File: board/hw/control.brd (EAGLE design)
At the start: 54.3 x 82.5 mm, 34 parts, among them T1 pn2222a, T2 pn2222a, T3 pn2222a, T4 pn2222a, T5 pn2222a, T6 pn2222a, T7 pn2222a, T8 pn2222a

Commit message: added missing power supply connector
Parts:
- added SV3: (no value), con-amp-mt:S02P
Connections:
- net +5V: now also SV3.1
- net 0V: now also SV3.2
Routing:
- net +5V: track 167.1 -> 177.8 mm
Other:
- board text added: "+5V"
- board text added: "GND"
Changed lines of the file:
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@@
 control board
 v1.0</text>
+<text x="86.995" y="58.42" size="1.778" layer="51" rot="R90">+5V</text>
+<text x="86.995" y="50.165" size="1.778" layer="51" rot="R90">GND</text>
 </plain>
 <attributes>
@@
 <element name="T1" library="transistor" package="TO92-CBE" value="pn2222a" x="73.66" y="62.23" smashed="yes">
 <attribute name="NAME" x="71.12" y="65.278" size="1.27" layer="25" ratio="10"/>
-<attribute name="VALUE" x="77.47" y="61.468" size="1.27" layer="27" ratio="10"/>
+<attribute name="VALUE" x="77.47" y="62.738" size="1.27" layer="27" ratio="10"/>
 </element>
 <element name="T2" library="transistor" package="TO92-CBE" value="pn2222a" x="71.12" y="54.61" smashed="yes">
@@
 <attribute name="NAME" x="44.45" y="35.179" size="1.27" layer="25" ratio="10" rot="R270"/>
 <attribute name="VALUE" x="44.323" y="46.609" size="1.27" layer="27" ratio="10" rot="R270"/>
+</element>
+<element name="SV3" library="con-amp-mt" package="S02P" value="" x="82.55" y="55.88" rot="R90">
+<attribute name="MPN" value="" x="82.55" y="55.88" size="1.778" layer="27" rot="R90" display="off"/>
+<attribute name="MF" value="" x="82.55" y="55.88" size="1.778" layer="27" rot="R90" display="off"/>
+<attribute name="OC_FARNELL" value="unknown" x="82.55" y="55.88" size="1.778" layer="27" rot="R90" display="off"/>
+<attribute name="OC_NEWARK" value="unknown" x="82.55" y="55.88" size="1.778" layer="27" rot="R90" display="off"/>
 </element>
 </elements>
@@
 <wire x1="40.64" y1="54.61" x2="40.64" y2="57.15" width="0.4064" layer="16"/>
 <wire x1="40.64" y1="57.15" x2="53.34" y2="69.85" width="0.4064" layer="16"/>
+<contactref element="SV3" pad="1"/>
+<wire x1="81.28" y1="67.31" x2="81.28" y2="58.4" width="0.4064" layer="16"/>
+<wire x1="81.28" y1="58.4" x2="82.55" y2="57.13" width="0.4064" layer="16"/>
 </signal>
 <signal name="0V">
@@
 <vertex x="35.56" y="80.01"/>
 </polygon>
+<contactref element="SV3" pad="2"/>
 </signal>
 <signal name="N$8">

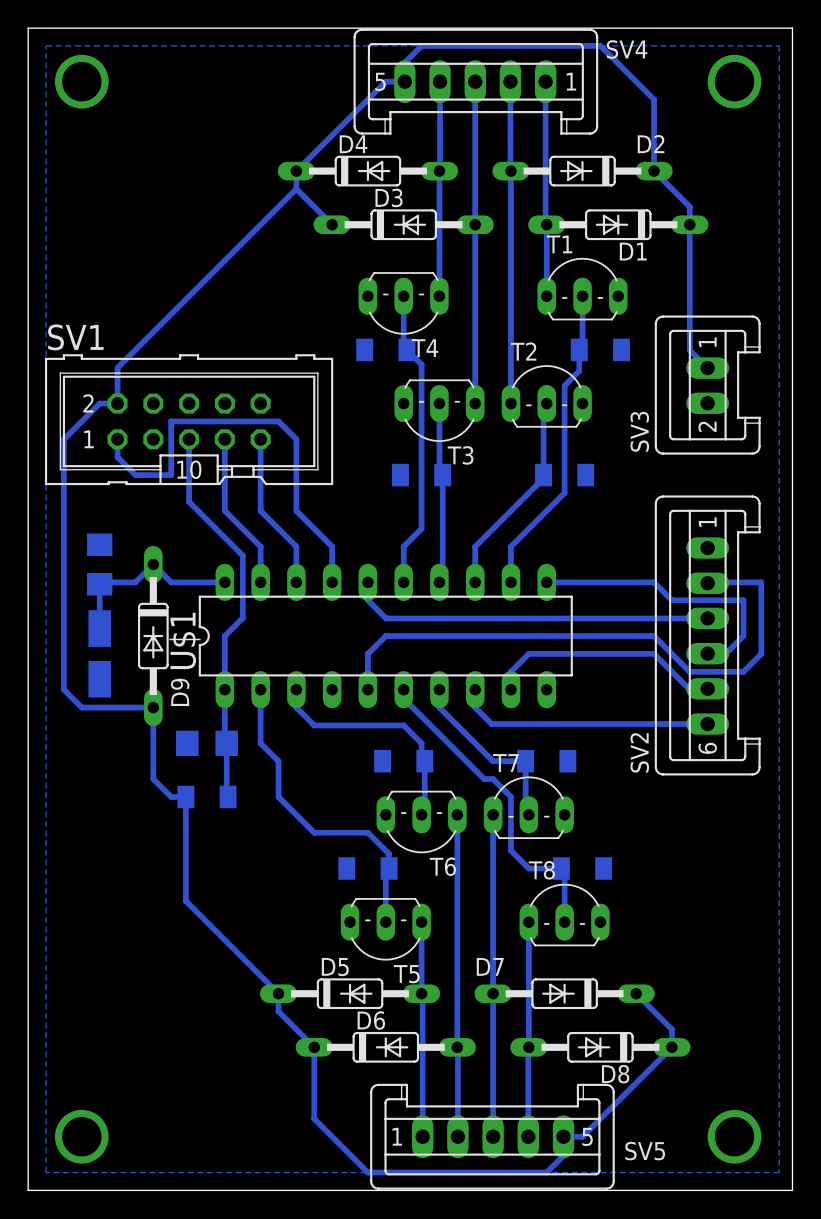
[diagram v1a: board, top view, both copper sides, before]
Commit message: added missing pull-up 100k Rs for all buttons
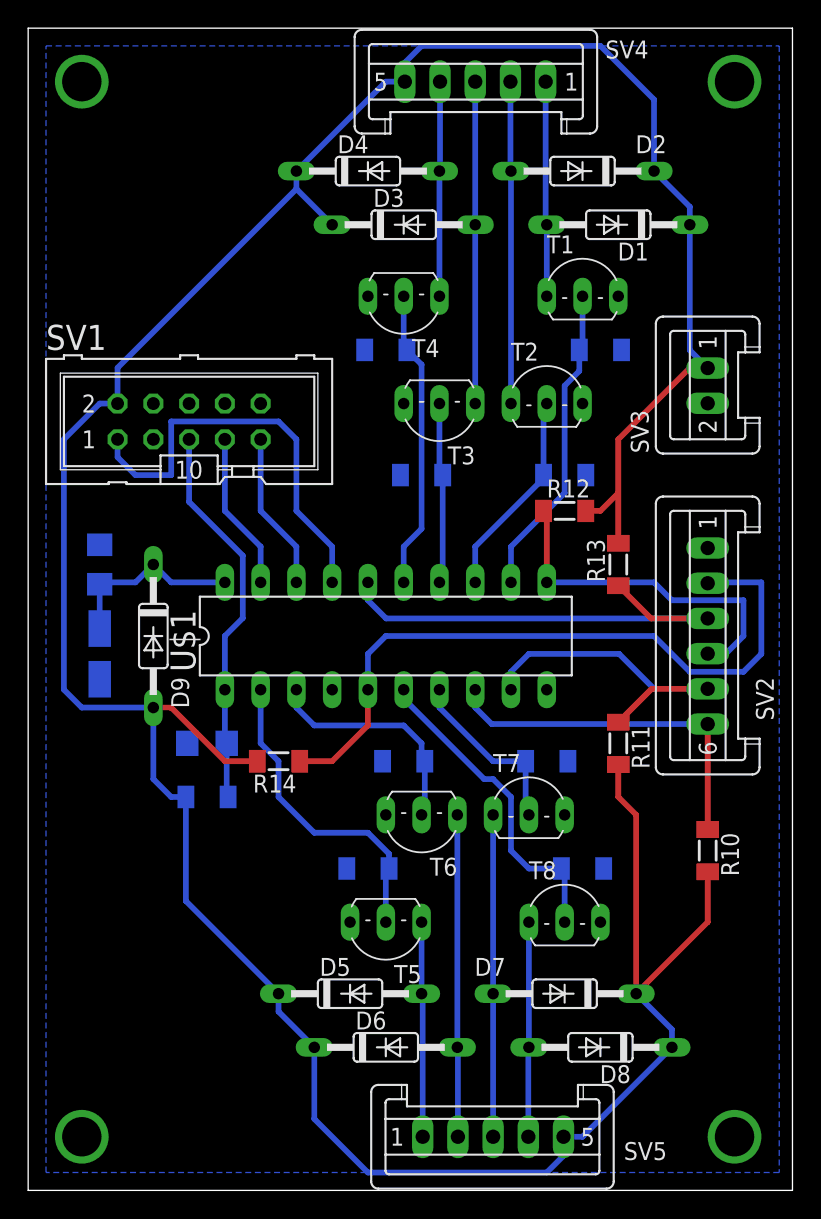
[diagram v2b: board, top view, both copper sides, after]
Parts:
- added R10, R11, R12, R13, R14: 100kR, rcl:MINI_MELF-0204W
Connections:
- net +5V: now also R10.2, R11.2, R12.2, R13.2, R14.2
- net N$22: now also R11.1
- net N$23: now also R12.1
- net N$24: now also R13.1
- net N$25: now also R14.1
- net N$3: now also R10.1
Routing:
- net +5V: track 177.8 -> 233.1 mm
- net N$25: track 41.5 -> 49.9 mm
- net N$3: track 18.3 -> 25.8 mm
- net N$22: track 16.8 -> 24.1 mm
- net N$24: track 25.9 -> 33.2 mm
- net N$23: track 20.1 -> 25.3 mm
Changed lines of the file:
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@@
 </element>
 <element name="D8" library="diode" package="DO35-10" value="1N4446" x="74.93" y="8.89" rot="R180"/>
-<element name="SV2" library="con-amp-mt" package="S06P" value="buttons" x="82.55" y="38.1" rot="R90">
+<element name="SV2" library="con-amp-mt" package="S06P" value="buttons" x="82.55" y="38.1" smashed="yes" rot="R90">
 <attribute name="MPN" value="" x="82.55" y="38.1" size="1.778" layer="27" rot="R90" display="off"/>
 <attribute name="MF" value="" x="82.55" y="38.1" size="1.778" layer="27" rot="R90" display="off"/>
 <attribute name="OC_NEWARK" value="unknown" x="82.55" y="38.1" size="1.778" layer="27" rot="R90" display="off"/>
 <attribute name="OC_FARNELL" value="unknown" x="82.55" y="38.1" size="1.778" layer="27" rot="R90" display="off"/>
+<attribute name="NAME" x="87.249" y="32.1072" size="1.27" layer="25" ratio="10" rot="R90"/>
+<attribute name="VALUE" x="78.359" y="35.4092" size="1.27" layer="27" ratio="10" rot="R90"/>
 </element>
 <element name="D9" library="diode" package="DO35-10" value="1N4446" x="43.18" y="38.1" smashed="yes" rot="R270">
@@
 <attribute name="OC_NEWARK" value="unknown" x="82.55" y="55.88" size="1.778" layer="27" rot="R90" display="off"/>
 </element>
+<element name="R10" library="rcl" package="MINI_MELF-0204W" value="100kR" x="82.55" y="22.86" rot="R270"/>
+<element name="R11" library="rcl" package="MINI_MELF-0204W" value="100kR" x="76.2" y="30.48" rot="R270"/>
+<element name="R12" library="rcl" package="MINI_MELF-0204W" value="100kR" x="72.39" y="46.99"/>
+<element name="R13" library="rcl" package="MINI_MELF-0204W" value="100kR" x="76.2" y="43.18" rot="R90"/>
+<element name="R14" library="rcl" package="MINI_MELF-0204W" value="100kR" x="52.07" y="29.21" rot="R180"/>
 </elements>
 <signals>
@@
 <wire x1="81.28" y1="67.31" x2="81.28" y2="58.4" width="0.4064" layer="16"/>
 <wire x1="81.28" y1="58.4" x2="82.55" y2="57.13" width="0.4064" layer="16"/>
+<contactref element="R10" pad="2"/>
+<contactref element="R11" pad="2"/>
+<contactref element="R12" pad="2"/>
+<contactref element="R13" pad="2"/>
+<contactref element="R14" pad="2"/>
+<wire x1="82.55" y1="21.36" x2="82.55" y2="17.78" width="0.4064" layer="1"/>
+<wire x1="82.55" y1="17.78" x2="77.47" y2="12.7" width="0.4064" layer="1"/>
+<wire x1="76.2" y1="26.67" x2="77.47" y2="25.4" width="0.4064" layer="1"/>
+<wire x1="77.47" y1="25.4" x2="77.47" y2="12.7" width="0.4064" layer="1"/>
+<wire x1="44.45" y1="33.02" x2="43.18" y2="33.02" width="0.4064" layer="1"/>
+<wire x1="76.2" y1="44.68" x2="76.2" y2="48.26" width="0.4064" layer="1"/>
+<wire x1="76.2" y1="48.26" x2="76.2" y2="52.07" width="0.4064" layer="1"/>
+<wire x1="76.2" y1="52.07" x2="81.28" y2="57.15" width="0.4064" layer="1"/>
+<wire x1="81.28" y1="57.15" x2="82.53" y2="57.15" width="0.4064" layer="1"/>
+<wire x1="82.53" y1="57.15" x2="82.55" y2="57.13" width="0.4064" layer="1"/>
+<wire x1="73.89" y1="46.99" x2="74.93" y2="46.99" width="0.4064" layer="1"/>
+<wire x1="74.93" y1="46.99" x2="76.2" y2="48.26" width="0.4064" layer="1"/>
+<wire x1="76.2" y1="28.98" x2="76.2" y2="26.67" width="0.4064" layer="1"/>
+<wire x1="50.57" y1="29.21" x2="48.26" y2="29.21" width="0.4064" layer="1"/>
+<wire x1="48.26" y1="29.21" x2="44.45" y2="33.02" width="0.4064" layer="1"/>
 </signal>
 <signal name="0V">
@@
 <wire x1="67.21" y1="31.85" x2="66.04" y2="33.02" width="0.4064" layer="16"/>
 <wire x1="66.04" y1="33.02" x2="66.04" y2="34.29" width="0.4064" layer="16"/>
+<contactref element="R10" pad="1"/>
+<wire x1="82.55" y1="24.36" x2="82.55" y2="31.85" width="0.4064" layer="1"/>
 </signal>
 <signal name="N$22">
 <contactref element="SV2" pad="5"/>
 <contactref element="U$1" pad="9"/>
-<wire x1="82.55" y1="34.35" x2="81.22" y2="34.35" width="0.4064" layer="16"/>
-<wire x1="81.22" y1="34.35" x2="78.74" y2="36.83" width="0.4064" layer="16"/>
-<wire x1="78.74" y1="36.83" x2="69.85" y2="36.83" width="0.4064" layer="16"/>
-<wire x1="69.85" y1="36.83" x2="68.58" y2="35.56" width="0.4064" layer="16"/>
-<wire x1="68.58" y1="35.56" x2="68.58" y2="34.29" width="0.4064" layer="16"/>
+<contactref element="R11" pad="1"/>
+<wire x1="82.55" y1="34.35" x2="78.57" y2="34.35" width="0.4064" layer="1"/>
+<wire x1="78.57" y1="34.35" x2="76.2" y2="31.98" width="0.4064" layer="1"/>
+<wire x1="68.58" y1="34.29" x2="68.58" y2="35.56" width="0.4064" layer="16"/>
+<wire x1="68.58" y1="35.56" x2="69.85" y2="36.83" width="0.4064" layer="16"/>
+<wire x1="69.85" y1="36.83" x2="76.26" y2="36.83" width="0.4064" layer="16"/>
+<wire x1="76.26" y1="36.83" x2="78.74" y2="34.35" width="0.4064" layer="16"/>
+<wire x1="78.74" y1="34.35" x2="82.55" y2="34.35" width="0.4064" layer="16"/>
 </signal>
 <signal name="N$23">
@@
 <wire x1="80.01" y1="40.64" x2="78.74" y2="41.91" width="0.4064" layer="16"/>
 <wire x1="78.74" y1="41.91" x2="71.12" y2="41.91" width="0.4064" layer="16"/>
+<contactref element="R12" pad="1"/>
+<wire x1="71.12" y1="41.91" x2="71.12" y2="46.76" width="0.4064" layer="1"/>
+<wire x1="71.12" y1="46.76" x2="70.89" y2="46.99" width="0.4064" layer="1"/>
 </signal>
 <signal name="N$24">
@@
 <wire x1="59.71" y1="39.35" x2="58.42" y2="40.64" width="0.4064" layer="16"/>
 <wire x1="58.42" y1="40.64" x2="58.42" y2="41.91" width="0.4064" layer="16"/>
+<contactref element="R13" pad="1"/>
+<wire x1="82.55" y1="39.35" x2="78.53" y2="39.35" width="0.4064" layer="1"/>
+<wire x1="78.53" y1="39.35" x2="76.2" y2="41.68" width="0.4064" layer="1"/>
 </signal>
 <signal name="N$25">
@@
 <wire x1="86.36" y1="41.91" x2="82.61" y2="41.91" width="0.4064" layer="16"/>
 <wire x1="82.61" y1="41.91" x2="82.55" y2="41.85" width="0.4064" layer="16"/>
+<contactref element="R14" pad="1"/>
+<wire x1="58.42" y1="34.29" x2="58.42" y2="31.75" width="0.4064" layer="1"/>
+<wire x1="58.42" y1="31.75" x2="55.88" y2="29.21" width="0.4064" layer="1"/>
+<wire x1="55.88" y1="29.21" x2="53.57" y2="29.21" width="0.4064" layer="1"/>
 </signal>
 <signal name="N$26">
